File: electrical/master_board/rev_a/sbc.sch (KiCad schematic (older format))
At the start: 30 parts, among them CN3 RPI_DSP_PWR;M1x2, CN94 RASPI;F2X20, Q23 POWER_PFET_GSD, Q24 2N7000;SOT23, SW2 BUTTON;6x3.5, U2 MCP7940;SOIC8, U3 CAT24C32;SOIC8, X1 32.768kHz9pF;3.2x1.5

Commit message: Fixed the schematic DRC errors.
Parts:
- removed Q23: POWER_PFET_GSD, Package_TO_SOT_SMD:SOT-23, symbol HR2:POWER_PFET_GSD
- added Q23: PFET_6A;SOT23, symbol HR2_MISC:Q_PWR_PMOS_GSD
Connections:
- wire segments 156 -> 153
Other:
- moved on the sheet: R67
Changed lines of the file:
@@
 $EndComp
 Wire Wire Line
-	4000 2100 4000 1650
+	4000 2100 4000 1600
 $Comp
 L Jumper:Jumper_3_Open JP9
@@
 L Device:R_US R67
 U 1 1 5FB84C0D
-P 1600 2800
+P 1700 2750
 AR Path="/5F4877FA/5FB84C0D" Ref="R67"  Part="1"
 AR Path="/5FA587FE/5FB84C0D" Ref="R?"  Part="1"
-F 0 "R67" H 1400 2900 50  0000 L CNN
-F 1 "100KΩ;1608" H 1100 2650 50  0000 L CNN
-F 2 "Resistor_SMD:R_0603_1608Metric" V 1640 2790 50  0001 C CNN
-F 3 "~" H 1600 2800 50  0001 C CNN
-	1    1600 2800
+F 0 "R67" H 1500 2850 50  0000 L CNN
+F 1 "100KΩ;1608" H 1200 2600 50  0000 L CNN
+F 2 "Resistor_SMD:R_0603_1608Metric" V 1740 2740 50  0001 C CNN
+F 3 "~" H 1700 2750 50  0001 C CNN
+	1    1700 2750
 	1    0    0    -1
 $EndComp
@@
 L Connector_Generic:Conn_01x02 CN3
 U 1 1 5FB885F0
-P 2900 2800
-F 0 "CN3" H 2800 2900 50  0000 L CNN
-F 1 "RPI_DSP_PWR;M1x2" H 2550 2600 50  0000 L CNN
-F 2 "Connector_PinHeader_2.54mm:PinHeader_1x02_P2.54mm_Vertical" H 2900 2800 50  0001 C CNN
-F 3 "~" H 2900 2800 50  0001 C CNN
-	1    2900 2800
+P 2900 2500
+F 0 "CN3" H 2800 2600 50  0000 L CNN
+F 1 "RPI_DSP_PWR;M1x2" H 2550 2300 50  0000 L CNN
+F 2 "Connector_PinHeader_2.54mm:PinHeader_1x02_P2.54mm_Vertical" H 2900 2500 50  0001 C CNN
+F 3 "~" H 2900 2500 50  0001 C CNN
+	1    2900 2500
 	1    0    0    -1
 $EndComp
@@
 	750  3150 750  1900
 Wire Wire Line
-	1400 3400 1000 3400
+	1400 3400 1100 3400
 Wire Wire Line
-	1700 2800 1800 2800
+	2500 4200 2500 2600
 Wire Wire Line
-	2500 4200 2500 2900
+	2500 2600 2700 2600
 Wire Wire Line
-	2500 2900 2700 2900
+	1800 2500 1700 2500
 Wire Wire Line
-	2600 2800 2700 2800
-$Comp
-L HR2:POWER_PFET_GSD Q?
-U 1 1 5FB5982B
-P 1800 2700
-AR Path="/5F52F39E/5FB5982B" Ref="Q?"  Part="1"
-AR Path="/5F4877FA/5FB5982B" Ref="Q23"  Part="1"
-F 0 "Q23" H 2050 2850 50  0000 C CNN
-F 1 "POWER_PFET_GSD" H 2100 2450 50  0000 C CNN
-F 2 "Package_TO_SOT_SMD:SOT-23" H 2000 2750 60  0001 L CNN
-F 3 "Power PFG (GSD pinout)" H 2000 2550 60  0001 L CNN
-F 4 "Power PFET (GSD pinout)" H 2000 2450 60  0001 L CNN "Field5"
-	1    1800 2700
-	1    0    0    -1
-$EndComp
-Wire Wire Line
-	1800 2700 1700 2700
-Wire Wire Line
-	1700 2700 1700 2550
-Wire Wire Line
-	1700 1650 4000 1650
+	1700 1600 4000 1600
 Wire Wire Line
 	750  4200 1700 4200
@@
 	750  1400 750  1600
 Wire Wire Line
-	1600 2650 1600 2550
+	1700 2600 1700 2500
+Connection ~ 1700 2500
 Wire Wire Line
-	1600 2550 1700 2550
-Connection ~ 1700 2550
+	1700 1600 1700 2500
 Wire Wire Line
-	1700 1650 1700 2550
+	1700 2900 1700 3000
+Connection ~ 1700 3000
 Wire Wire Line
-	1600 2950 1600 3050
-Wire Wire Line
-	1600 3050 1700 3050
-Connection ~ 1700 3050
-Wire Wire Line
-	1700 3050 1700 2800
-Wire Wire Line
-	1700 3050 1700 3200
+	1700 3000 1700 3200
 Wire Wire Line
 	750  4100 750  4200
@@
 Raspberry Pi Display\nPower Enable Circuit
 Wire Wire Line
-	1000 3400 1000 2550
+	1100 3400 1100 2500
 Wire Wire Line
-	1000 2550 1300 2550
+	1100 2500 1300 2500
 Wire Wire Line
-	1300 2550 1300 1500
+	1300 2500 1300 1500
 Wire Wire Line
 	1300 1500 4600 1500
@@
 Wire Wire Line
 	4600 3000 3900 3000
-Connection ~ 1000 3400
+Connection ~ 1100 3400
 Wire Wire Line
-	1000 3400 900  3400
+	1100 3400 900  3400
 Text Notes 500  4650 0    50   ~ 0
 Notes:\n1. Jumper controlls default display Power On/Off.\n2. Transistor shifts from 3.3V to 5V Gate On/Off.\n3. Jumper provides switched 5V to Ras Pi Display.\n4. Raspberry Pi can override jumper.
@@
 Wire Wire Line
 	4800 2900 5000 2900
+$Comp
+L HR2_MISC:Q_PWR_PMOS_GSD Q23
+U 1 1 5FF1459E
+P 2000 2600
+F 0 "Q23" V 1900 2500 50  0000 C CNN
+F 1 "PFET_6A;SOT23" V 2250 2600 50  0000 C CNN
+F 2 "" H 2200 2700 50  0001 C CNN
+F 3 "~" H 2000 2600 50  0001 C CNN
+	1    2000 2600
+	0    1    -1   0
+$EndComp
+Wire Wire Line
+	1700 3000 2000 3000
+Wire Wire Line
+	2000 3000 2000 2800
+Wire Wire Line
+	2200 2500 2700 2500
 $EndSCHEMATC

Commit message: Moved Power Supply.
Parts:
- Q23: footprint (none) -> Package_TO_SOT_SMD:SOT-23
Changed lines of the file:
@@
 F 0 "Q23" V 1900 2500 50  0000 C CNN
 F 1 "PFET_6A;SOT23" V 2250 2600 50  0000 C CNN
-F 2 "" H 2200 2700 50  0001 C CNN
+F 2 "Package_TO_SOT_SMD:SOT-23" H 2200 2700 50  0001 C CNN
 F 3 "~" H 2000 2600 50  0001 C CNN
 	1    2000 2600

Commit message: Changed more parts to 1005 size and R9 value
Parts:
- C10, C8: value 10pF;1608 -> 0.1µF;1005; footprint Capacitor_SMD:C_0603_1608Metric -> Capacitor_SMD:C_0402_1005Metric
- C7, C9: value 16pF;1608 -> 16pF;1005; footprint Capacitor_SMD:C_0603_1608Metric -> Capacitor_SMD:C_0402_1005Metric
- R10, R8: value 3.9KΩ;1608 -> 3.9KΩ;1005; footprint Resistor_SMD:R_0603_1608Metric -> Resistor_SMD:R_0402_1005Metric
- R11: value 1KΩ;1608 -> 1KΩ;1005; footprint Resistor_SMD:R_0603_1608Metric -> Resistor_SMD:R_0402_1005Metric
- R12, R13: value 4.7KΩ;1608 -> 4.7KΩ;1005; footprint Resistor_SMD:R_0603_1608Metric -> Resistor_SMD:R_0402_1005Metric
- R14, R6, R66, R67, R7: value 100KΩ;1608 -> 100KΩ;1005; footprint Resistor_SMD:R_0603_1608Metric -> Resistor_SMD:R_0402_1005Metric
- R9: value 470KΩ;1608 -> 470Ω;1608
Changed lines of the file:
@@
 AR Path="/5FA587FE/5F5097A4" Ref="C?"  Part="1"
 F 0 "C9" H 7150 3550 50  0000 L CNN
-F 1 "16pF;1608" H 7300 3350 50  0000 L CNN
-F 2 "Capacitor_SMD:C_0603_1608Metric" H 7338 3300 50  0001 C CNN
+F 1 "16pF;1005" H 7300 3350 50  0000 L CNN
+F 2 "Capacitor_SMD:C_0402_1005Metric" H 7338 3300 50  0001 C CNN
 F 3 "~" H 7300 3450 50  0001 C CNN
 	1    7300 3450
@@
 AR Path="/5FA587FE/5F509B6B" Ref="C?"  Part="1"
 F 0 "C7" H 5850 3550 50  0000 L CNN
-F 1 "16pF;1608" H 6000 3350 50  0000 L CNN
-F 2 "Capacitor_SMD:C_0603_1608Metric" H 6038 3300 50  0001 C CNN
+F 1 "16pF;1005" H 6000 3350 50  0000 L CNN
+F 2 "Capacitor_SMD:C_0402_1005Metric" H 6038 3300 50  0001 C CNN
 F 3 "~" H 6000 3450 50  0001 C CNN
 	1    6000 3450
@@
 AR Path="/5FA587FE/5F510131" Ref="R?"  Part="1"
 F 0 "R8" H 5350 2050 50  0000 L CNN
-F 1 "3.9KΩ;1608" H 5550 1850 50  0000 L CNN
-F 2 "Resistor_SMD:R_0603_1608Metric" V 5540 1940 50  0001 C CNN
+F 1 "3.9KΩ;1005" H 5550 1850 50  0000 L CNN
+F 2 "Resistor_SMD:R_0402_1005Metric" V 5540 1940 50  0001 C CNN
 F 3 "~" H 5500 1950 50  0001 C CNN
 	1    5500 1950
@@
 AR Path="/5FA587FE/5F510F46" Ref="R?"  Part="1"
 F 0 "R10" H 5950 2050 50  0000 L CNN
-F 1 "3.9KΩ;1608" H 6150 1850 50  0000 L CNN
-F 2 "Resistor_SMD:R_0603_1608Metric" V 6140 1940 50  0001 C CNN
+F 1 "3.9KΩ;1005" H 6150 1850 50  0000 L CNN
+F 2 "Resistor_SMD:R_0402_1005Metric" V 6140 1940 50  0001 C CNN
 F 3 "~" H 6100 1950 50  0001 C CNN
 	1    6100 1950
@@
 AR Path="/5FA587FE/5F50DB19" Ref="R?"  Part="1"
 F 0 "R13" H 6750 5150 50  0000 L CNN
-F 1 "4.7KΩ;1608" H 6950 4950 50  0000 L CNN
-F 2 "Resistor_SMD:R_0603_1608Metric" V 6940 5040 50  0001 C CNN
+F 1 "4.7KΩ;1005" H 6950 4950 50  0000 L CNN
+F 2 "Resistor_SMD:R_0402_1005Metric" V 6940 5040 50  0001 C CNN
 F 3 "~" H 6900 5050 50  0001 C CNN
 	1    6900 5050
@@
 AR Path="/5FA587FE/5F50E10E" Ref="R?"  Part="1"
 F 0 "R14" H 7350 5150 50  0000 L CNN
-F 1 "100KΩ;1608" H 7550 4950 50  0000 L CNN
-F 2 "Resistor_SMD:R_0603_1608Metric" V 7540 5040 50  0001 C CNN
+F 1 "100KΩ;1005" H 7550 4950 50  0000 L CNN
+F 2 "Resistor_SMD:R_0402_1005Metric" V 7540 5040 50  0001 C CNN
 F 3 "~" H 7500 5050 50  0001 C CNN
 	1    7500 5050
@@
 AR Path="/5FA587FE/5F50FCF9" Ref="R?"  Part="1"
 F 0 "R12" H 6150 5150 50  0000 L CNN
-F 1 "4.7KΩ;1608" H 6350 4950 50  0000 L CNN
-F 2 "Resistor_SMD:R_0603_1608Metric" V 6340 5040 50  0001 C CNN
+F 1 "4.7KΩ;1005" H 6350 4950 50  0000 L CNN
+F 2 "Resistor_SMD:R_0402_1005Metric" V 6340 5040 50  0001 C CNN
 F 3 "~" H 6300 5050 50  0001 C CNN
 	1    6300 5050
@@
 AR Path="/5FA587FE/5F58D7BC" Ref="R?"  Part="1"
 F 0 "R6" H 4450 4950 50  0000 L CNN
-F 1 "100KΩ;1608" H 4650 4750 50  0000 L CNN
-F 2 "Resistor_SMD:R_0603_1608Metric" V 4640 4840 50  0001 C CNN
+F 1 "100KΩ;1005" H 4650 4750 50  0000 L CNN
+F 2 "Resistor_SMD:R_0402_1005Metric" V 4640 4840 50  0001 C CNN
 F 3 "~" H 4600 4850 50  0001 C CNN
 	1    4600 4850
@@
 AR Path="/5FA587FE/5FAF8B92" Ref="R?"  Part="1"
 F 0 "R11" V 4800 4150 50  0000 L CNN
-F 1 "1KΩ;1608" V 5000 4050 50  0000 L CNN
-F 2 "Resistor_SMD:R_0603_1608Metric" V 4940 4190 50  0001 C CNN
+F 1 "1KΩ;1005" V 5000 4050 50  0000 L CNN
+F 2 "Resistor_SMD:R_0402_1005Metric" V 4940 4190 50  0001 C CNN
 F 3 "~" H 4900 4200 50  0001 C CNN
 	1    4900 4200
@@
 AR Path="/5FA587FE/5FB254F3" Ref="R?"  Part="1"
 F 0 "R9" H 5350 4850 50  0000 L CNN
-F 1 "470KΩ;1608" H 5550 4650 50  0000 L CNN
+F 1 "470Ω;1608" H 5550 4650 50  0000 L CNN
 F 2 "Resistor_SMD:R_0603_1608Metric" V 5540 4740 50  0001 C CNN
 F 3 "~" H 5500 4750 50  0001 C CNN
@@
 AR Path="/5FA587FE/5F917643" Ref="R?"  Part="1"
 F 0 "R7" H 5150 5250 50  0000 L CNN
-F 1 "100KΩ;1608" H 4800 5000 50  0000 L CNN
-F 2 "Resistor_SMD:R_0603_1608Metric" V 5340 5140 50  0001 C CNN
+F 1 "100KΩ;1005" H 4800 5000 50  0000 L CNN
+F 2 "Resistor_SMD:R_0402_1005Metric" V 5340 5140 50  0001 C CNN
 F 3 "~" H 5300 5150 50  0001 C CNN
 	1    5300 5150
@@
 AR Path="/5FA587FE/5FA44A8F" Ref="C?"  Part="1"
 F 0 "C10" H 7150 4050 50  0000 L CNN
-F 1 "10pF;1608" H 7300 3850 50  0000 L CNN
-F 2 "Capacitor_SMD:C_0603_1608Metric" H 7338 3800 50  0001 C CNN
+F 1 "0.1µF;1005" H 7300 3850 50  0000 L CNN
+F 2 "Capacitor_SMD:C_0402_1005Metric" H 7338 3800 50  0001 C CNN
 F 3 "~" H 7300 3950 50  0001 C CNN
 	1    7300 3950
@@
 AR Path="/5FA587FE/5FA24EA3" Ref="C?"  Part="1"
 F 0 "C8" H 6700 2250 50  0000 L CNN
-F 1 "10pF;1608" H 6250 2050 50  0000 L CNN
-F 2 "Capacitor_SMD:C_0603_1608Metric" H 6738 2000 50  0001 C CNN
+F 1 "0.1µF;1005" H 6250 2050 50  0000 L CNN
+F 2 "Capacitor_SMD:C_0402_1005Metric" H 6738 2000 50  0001 C CNN
 F 3 "~" H 6700 2150 50  0001 C CNN
 	1    6700 2150
@@
 AR Path="/5FA587FE/5FB84C0D" Ref="R?"  Part="1"
 F 0 "R67" H 1500 2850 50  0000 L CNN
-F 1 "100KΩ;1608" H 1200 2600 50  0000 L CNN
-F 2 "Resistor_SMD:R_0603_1608Metric" V 1740 2740 50  0001 C CNN
+F 1 "100KΩ;1005" H 1200 2600 50  0000 L CNN
+F 2 "Resistor_SMD:R_0402_1005Metric" V 1740 2740 50  0001 C CNN
 F 3 "~" H 1700 2750 50  0001 C CNN
 	1    1700 2750
@@
 AR Path="/5FA587FE/5FB69F2A" Ref="R?"  Part="1"
 F 0 "R66" H 600 4050 50  0000 L CNN
-F 1 "100KΩ;1608" H 800 3850 50  0000 L CNN
-F 2 "Resistor_SMD:R_0603_1608Metric" V 790 3940 50  0001 C CNN
+F 1 "100KΩ;1005" H 800 3850 50  0000 L CNN
+F 2 "Resistor_SMD:R_0402_1005Metric" V 790 3940 50  0001 C CNN
 F 3 "~" H 750 3950 50  0001 C CNN
 	1    750  3950

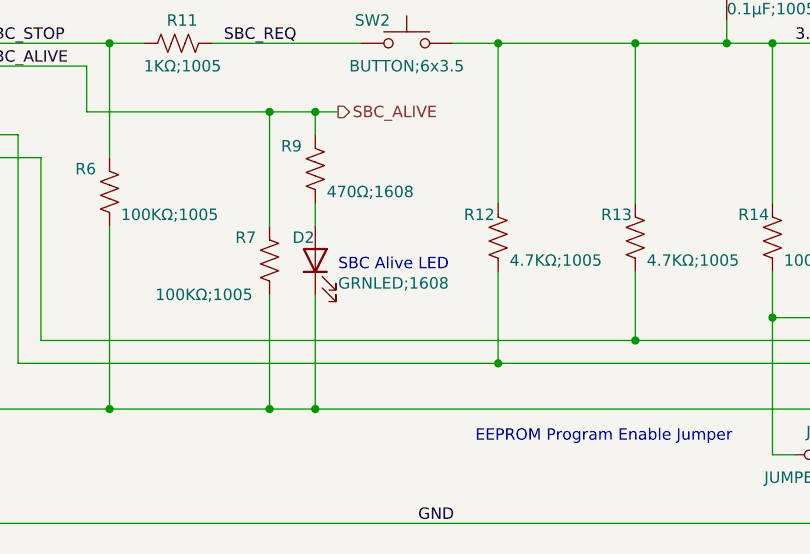
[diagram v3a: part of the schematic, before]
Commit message: Worked on JLCPCB BOM generation.
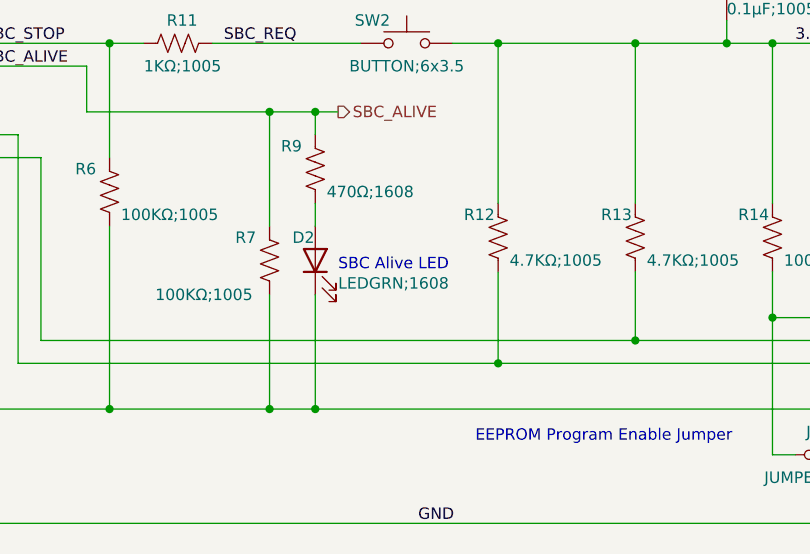
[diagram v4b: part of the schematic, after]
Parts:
- D2: value GRNLED;1608 -> LEDGRN;1608
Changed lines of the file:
@@
 AR Path="/5F4877FA/5FB21992" Ref="D2"  Part="1"
 F 0 "D2" V 5600 5250 50  0000 R CNN
-F 1 "GRNLED;1608" V 5400 5050 50  0000 R CNN
+F 1 "LEDGRN;1608" V 5400 5050 50  0000 R CNN
 F 2 "LED_SMD:LED_0603_1608Metric" H 5500 5150 50  0001 C CNN
 F 3 "~" H 5500 5150 50  0001 C CNN

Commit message: JLCPCB BOM is in better shape.
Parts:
- removed Q24: 2N7000;SOT23, Package_TO_SOT_SMD:SOT-23, symbol Transistor_FET:2N7000
- added Q24: 2N7002;SOT23, Package_TO_SOT_SMD:SOT-23, symbol Transistor_FET:2N7002
- C7: value 16pF;1005 -> 16pF;1608; footprint Capacitor_SMD:C_0402_1005Metric -> Capacitor_SMD:C_0603_1608Metric
- C9: value 16pF;1005 -> 16pF;1608
- Q23: value PFET_6A;SOT23 -> PFET_6A_GSD;SOT23
- X1: footprint Crystal:Crystal_SMD_5032-2Pin_5.0x3.2mm -> Crystal:Crystal_SMD_3215-2Pin_3.2x1.5mm
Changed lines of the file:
@@
 F 0 "X1" H 6650 3350 50  0000 C CNN
 F 1 "32.768kHz9pF;3.2x1.5" H 6600 3050 50  0000 C CNN
-F 2 "Crystal:Crystal_SMD_5032-2Pin_5.0x3.2mm" H 6650 3200 50  0001 C CNN
+F 2 "Crystal:Crystal_SMD_3215-2Pin_3.2x1.5mm" H 6650 3200 50  0001 C CNN
 F 3 "~" H 6650 3200 50  0001 C CNN
 	1    6650 3200
@@
 AR Path="/5FA587FE/5F5097A4" Ref="C?"  Part="1"
 F 0 "C9" H 7150 3550 50  0000 L CNN
-F 1 "16pF;1005" H 7300 3350 50  0000 L CNN
+F 1 "16pF;1608" H 7300 3350 50  0000 L CNN
 F 2 "Capacitor_SMD:C_0402_1005Metric" H 7338 3300 50  0001 C CNN
 F 3 "~" H 7300 3450 50  0001 C CNN
@@
 AR Path="/5FA587FE/5F509B6B" Ref="C?"  Part="1"
 F 0 "C7" H 5850 3550 50  0000 L CNN
-F 1 "16pF;1005" H 6000 3350 50  0000 L CNN
-F 2 "Capacitor_SMD:C_0402_1005Metric" H 6038 3300 50  0001 C CNN
+F 1 "16pF;1608" H 6000 3350 50  0000 L CNN
+F 2 "Capacitor_SMD:C_0603_1608Metric" H 6038 3300 50  0001 C CNN
 F 3 "~" H 6000 3450 50  0001 C CNN
 	1    6000 3450
@@
 $EndComp
 $Comp
-L Transistor_FET:2N7000 Q?
-U 1 1 5FB7067A
-P 1600 3400
-AR Path="/5F79BC00/5FB7067A" Ref="Q?"  Part="1"
-AR Path="/5FA4A874/5FB7067A" Ref="Q?"  Part="1"
-AR Path="/5FAD82EE/5FB7067A" Ref="Q?"  Part="1"
-AR Path="/5F8C2F57/5FB7067A" Ref="Q?"  Part="1"
-AR Path="/5F4877FA/5FB7067A" Ref="Q24"  Part="1"
-F 0 "Q24" H 1500 3550 50  0000 L CNN
-F 1 "2N7000;SOT23" H 1750 3250 50  0000 L CNN
-F 2 "Package_TO_SOT_SMD:SOT-23" H 1800 3325 50  0001 L CIN
-F 3 "https://www.fairchildsemi.com/datasheets/2N/2N7000.pdf" H 1600 3400 50  0001 L CNN
-	1    1600 3400
-	1    0    0    -1
-$EndComp
-$Comp
 L Device:R_US R67
 U 1 1 5FB84C0D
@@
 	1400 3400 1100 3400
 Wire Wire Line
-	2500 4200 2500 2600
-Wire Wire Line
 	2500 2600 2700 2600
 Wire Wire Line
@@
 	1    0    0    -1
 $EndComp
-Text Notes 1900 2300 0    50   ~ 0
+Text Notes 1750 2250 0    50   ~ 0
 Raspberry Pi Display\nPower Enable Circuit
 Wire Wire Line
@@
 P 2000 2600
 F 0 "Q23" V 1900 2500 50  0000 C CNN
-F 1 "PFET_6A;SOT23" V 2250 2600 50  0000 C CNN
+F 1 "PFET_6A_GSD;SOT23" V 2250 2700 50  0000 C CNN
 F 2 "Package_TO_SOT_SMD:SOT-23" H 2200 2700 50  0001 C CNN
 F 3 "~" H 2000 2600 50  0001 C CNN
@@
 Wire Wire Line
 	2200 2500 2700 2500
+Wire Wire Line
+	2500 2600 2500 4200
+$Comp
+L Transistor_FET:2N7002 Q24
+U 1 1 5FE943A9
+P 1600 3400
+F 0 "Q24" H 1450 3550 50  0000 L CNN
+F 1 "2N7002;SOT23" H 1750 3300 50  0000 L CNN
+F 2 "Package_TO_SOT_SMD:SOT-23" H 1800 3325 50  0001 L CIN
+F 3 "https://www.onsemi.com/pub/Collateral/NDS7002A-D.PDF" H 1600 3400 50  0001 L CNN
+	1    1600 3400
+	1    0    0    -1
+$EndComp
 $EndSCHEMATC

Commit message: JLCPCB Footprints are both consistent and available.
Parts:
- C7: value 16pF;1608 -> 15pF;1608
- C9: value 16pF;1608 -> 15pF;1608; footprint Capacitor_SMD:C_0402_1005Metric -> Capacitor_SMD:C_0603_1608Metric
- SW2: value BUTTON;6x3.5 -> BUTTON;6x6; footprint HR2:BUTTON_6x3.5 -> Button_Switch_SMD:SW_Push_1P1T_NO_6x6mm_H9.5mm
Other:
- note added: "Real Time Clock Notes:\n1. Reference: https://suntsu.com/crystal-load-capacitance/\n2. Real Time Clock is needed to set the operatiing system time need for\n ROS (Robot Operating System.)\n3. The crystal load capacitor calculations are:\n A. Cld = (C1 x C2) / (C1 + C2) + 5pF, where:\n 5pF = stray PCB trace capacitance,\n Cld = desired crystal load capacitence and\n C1 and C2 are two capactors con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"
- note removed: "Real Time Clock Notes:\n1. Real Time Clock is needed to set the operatiing system time need for\n ROS (Robot Operating System.)\n2. The crystal load capacitor calculations are:\n A. Cld = (C1 x C2) / (C1 + C2), where:\n Cld = crystal load capacitence (i.e. 7-9pF) assume 8pF\n C1 and C2 are two capactors connected to ground, one to each crystal side.\n B. Assume C1 = C2 and call it C.\n C. Cld = (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"
- moved on the sheet: BT1, C10, C7, C8, C9, CN94, D2, JP1, R10, R11, R12, R13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

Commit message: Changed various resistor sizes and values
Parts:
- R9: value 470Ω;1608 -> 33Ω;1005; footprint Resistor_SMD:R_0603_1608Metric -> Resistor_SMD:R_0402_1005Metric
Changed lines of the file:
@@
 AR Path="/5FA587FE/5FB254F3" Ref="R?"  Part="1"
 F 0 "R9" H 5350 5200 50  0000 L CNN
-F 1 "470Ω;1608" H 5550 5000 50  0000 L CNN
-F 2 "Resistor_SMD:R_0603_1608Metric" V 5540 5090 50  0001 C CNN
+F 1 "33Ω;1005" H 5550 5000 50  0000 L CNN
+F 2 "Resistor_SMD:R_0402_1005Metric" V 5540 5090 50  0001 C CNN
 F 3 "~" H 5500 5100 50  0001 C CNN
 	1    5500 5100

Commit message: Gave LED's their own ground return. Cleaned up Silk layer.
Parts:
- X1: value 32.768kHz9pF;3.2x1.5 -> 32.768kHz12.5pF;3.2x1.5
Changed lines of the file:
@@
 AR Path="/5FA587FE/5F4F5A10" Ref="X?"  Part="1"
 F 0 "X1" H 6650 3700 50  0000 C CNN
-F 1 "32.768kHz9pF;3.2x1.5" H 6600 3400 50  0000 C CNN
+F 1 "32.768kHz12.5pF;3.2x1.5" H 6600 3400 50  0000 C CNN
 F 2 "Crystal:Crystal_SMD_3215-2Pin_3.2x1.5mm" H 6650 3550 50  0001 C CNN
 F 3 "~" H 6650 3550 50  0001 C CNN
